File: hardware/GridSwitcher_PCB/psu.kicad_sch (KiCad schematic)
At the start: 36 parts, among them IC1 INA237AIDGSR, IC2 UCC27536DBVR, IC6 P3T1755DPZ, J7 +24V, J8 Battery, Q18 IRF4905

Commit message: -enh made some progress on pcb/fp design
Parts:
- removed Q18: IRF4905, Package_TO_SOT_SMD:TO-263-3_TabPin2, symbol Transistor_FET:IRF4905
- added J11: +24V, Connector_PinHeader_2.54mm:PinHeader_1x02_P2.54mm_Vertical, symbol Connector:Conn_01x02_Pin
- added J14: +3.3V, Connector_PinHeader_2.54mm:PinHeader_1x02_P2.54mm_Vertical, symbol Connector:Conn_01x02_Pin
- added J15: +5V, Connector_PinHeader_2.54mm:PinHeader_1x02_P2.54mm_Vertical, symbol Connector:Conn_01x02_Pin
- added Q17: DMP3013SFV, Package_SON:Diodes_PowerDI3333-8, symbol Transistor_FET:DMP3013SFV
- F3, F4, F5: footprint (none) -> Fuse:Fuse_2920_7451Metric_Pad2.10x5.45mm_HandSolder
- IC1: footprint INA237:SOP50P490X110-10N -> Library:SOP50P490X110-10N
- IC2: footprint (none) -> Library:SOT95P280X145-5N
- IC6: footprint (none) -> Library:P3T1755DPZ
- J7: footprint TerminalBlock:TerminalBlock_bornier-2_P5.08mm -> Connector_BarrelJack:BarrelJack_Wuerth_6941xx301002
- L1, L2: footprint (none) -> Inductor_SMD:L_Bourns-SRN4018
- PS1, PS2: footprint (none) -> Library:R78K3305
- R102, R96, R98: footprint (none) -> Resistor_SMD:R_0603_1608Metric_Pad0.98x0.95mm_HandSolder
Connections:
- net +24V: now also J11.1 (Pin_1)
- net +3V3: now also J14.1 (Pin_1)
- net +5V: now also J15.1 (Pin_1)
- net GND: now also J11.2 (Pin_2), J14.2 (Pin_2), J15.2 (Pin_2)
- net at IC2.4 (OUT), R97.2: now also Q17.4 (G)
- net at F4.2, IC2.5 (VDD), R97.1: now also Q17.1 (S), Q17.2 (S), Q17.3 (S)
- net at R99.1: now also Q17.5 (D)

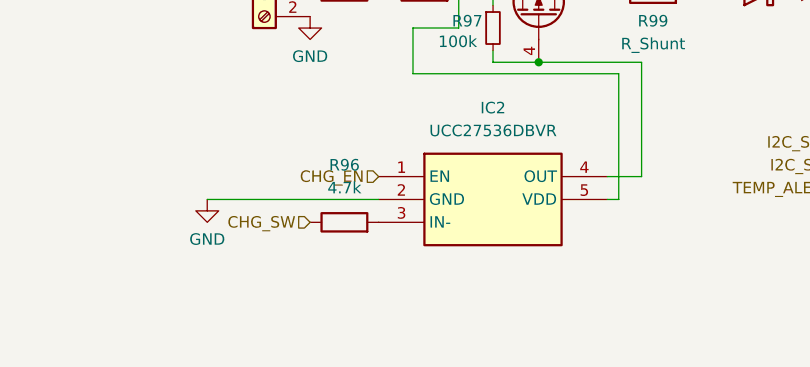
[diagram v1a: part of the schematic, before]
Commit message: -add some changes to schematic, tested the interfaces (uart, spi and i2c) with some test code
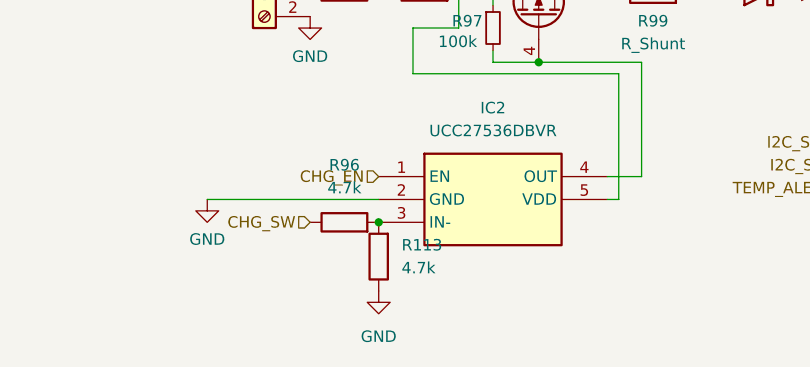
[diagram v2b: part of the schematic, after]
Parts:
- added R113: 4.7k, Resistor_SMD:R_0603_1608Metric_Pad0.98x0.95mm_HandSolder, symbol Device:R
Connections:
- net GND: now also R113.1
- net at IC2.3 (IN-), R96.2: now also R113.2

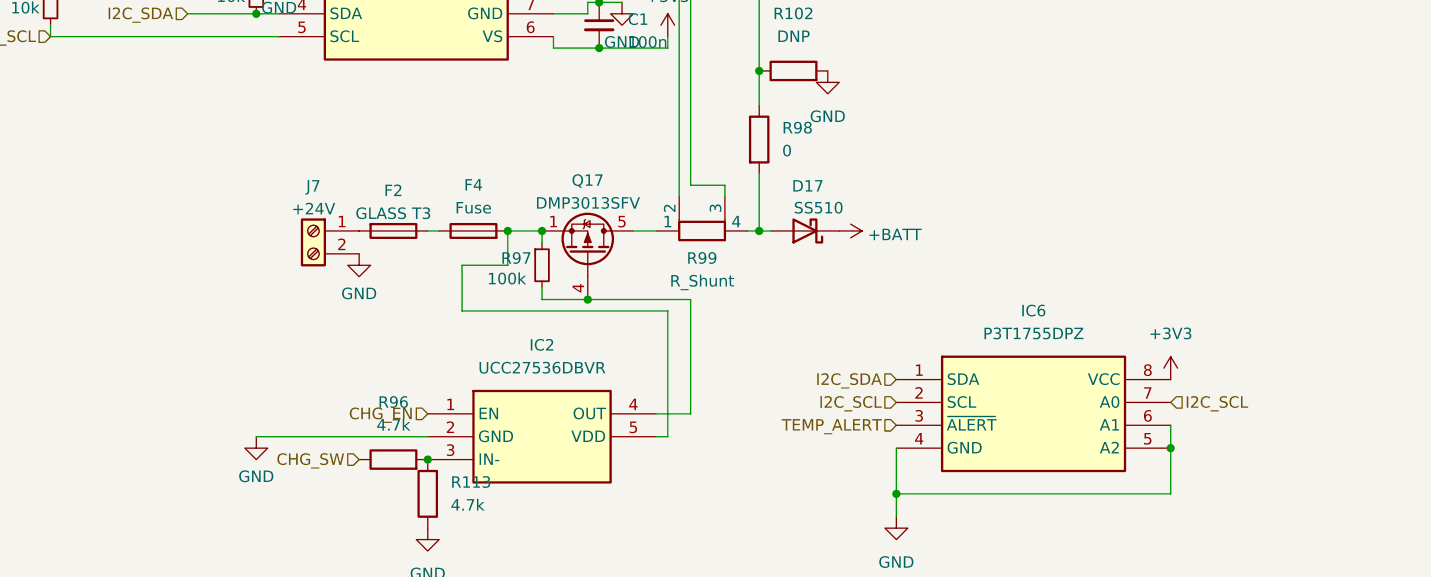
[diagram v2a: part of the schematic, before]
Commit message: -add some more pinning changes, add rts flow control for rs485
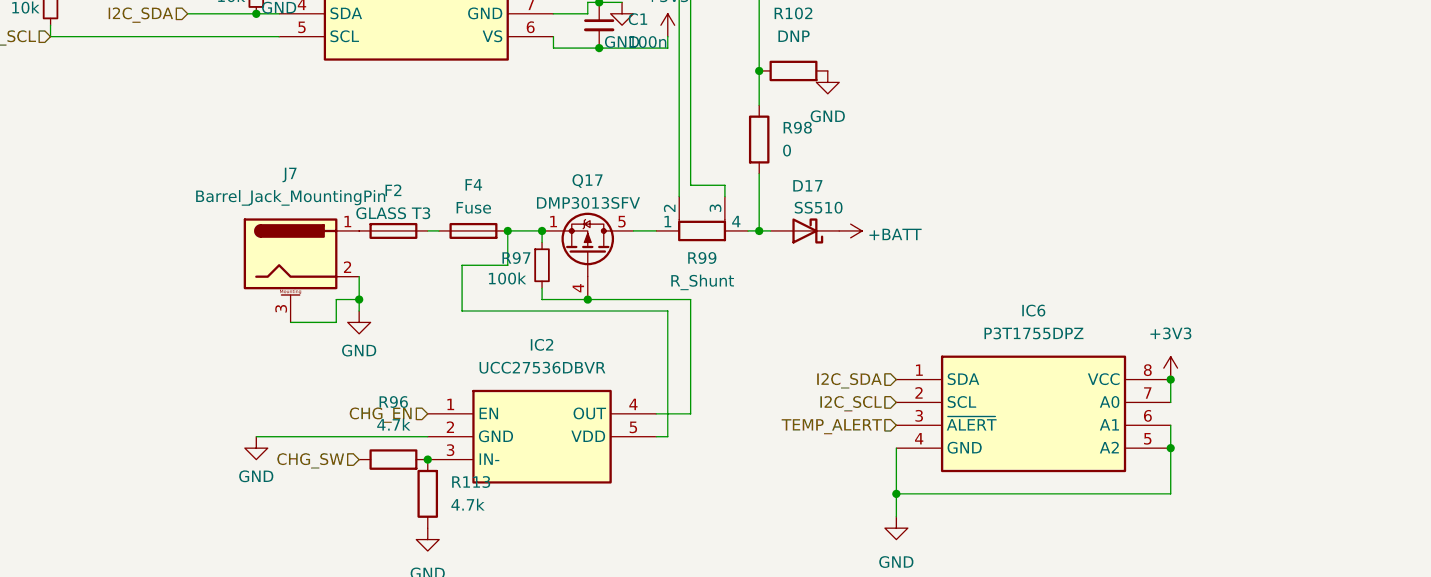
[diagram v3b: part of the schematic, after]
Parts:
- removed J7: +24V, Connector_BarrelJack:BarrelJack_Wuerth_6941xx301002, symbol Connector:Screw_Terminal_01x02
- added J7: Barrel_Jack_MountingPin, Connector_BarrelJack:BarrelJack_Wuerth_6941xx301002, symbol Connector:Barrel_Jack_MountingPin
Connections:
- net +3V3: now also IC6.7 (A0)
- net GND: now also J7.2, J7.3 (MountPin)
- net I2C_SCL: no longer IC6.7 (A0)
- net at F2.2: now also J7.1
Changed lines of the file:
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@@
 	)
 	(junction
+		(at 62.23 114.3)
+		(diameter 0)
+		(color 0 0 0 0)
+	)
+	(junction
 		(at 88.9 86.36)
 		(diameter 0)
@@
 	)
 	(junction
+		(at 152.4 123.19)
+		(diameter 0)
+		(color 0 0 0 0)
+	)
+	(junction
 		(at 194.31 44.45)
 		(diameter 0)
@@
 	(wire
 		(pts
+			(xy 59.69 116.84) (xy 59.69 114.3)
+		)
+		(stroke
+			(width 0)
+			(type default)
+		)
+	)
+	(wire
+		(pts
 			(xy 215.9 49.53) (xy 218.44 49.53)
 		)
@@
 	(wire
 		(pts
+			(xy 54.61 116.84) (xy 59.69 116.84)
+		)
+		(stroke
+			(width 0)
+			(type default)
+		)
+	)
+	(wire
+		(pts
 			(xy 118.11 43.18) (xy 116.84 43.18)
 		)
@@
 	(wire
 		(pts
+			(xy 62.23 115.57) (xy 62.23 114.3)
+		)
+		(stroke
+			(width 0)
+			(type default)
+		)
+	)
+	(wire
+		(pts
 			(xy 87.63 114.3) (xy 99.06 114.3)
 		)
@@
 	(wire
 		(pts
+			(xy 62.23 114.3) (xy 62.23 111.76)
+		)
+		(stroke
+			(width 0)
+			(type default)
+		)
+	)
+	(wire
+		(pts
 			(xy 27.94 85.09) (xy 27.94 83.82)
 		)
@@
 	(wire
 		(pts
+			(xy 59.69 114.3) (xy 62.23 114.3)
+		)
+		(stroke
+			(width 0)
+			(type default)
+		)
+	)
+	(wire
+		(pts
 			(xy 152.4 128.27) (xy 152.4 130.81)
 		)
@@
 	(wire
 		(pts
+			(xy 152.4 123.19) (xy 152.4 125.73)
+		)
+		(stroke
+			(width 0)
+			(type default)
+		)
+	)
+	(wire
+		(pts
 			(xy 45.72 78.74) (xy 45.72 80.01)
 		)
@@
 		)
 	)
-	(hierarchical_label "I2C_SCL"
-		(shape input)
-		(at 152.4 125.73 0)
-		(fields_autoplaced yes)
-		(effects
-			(font
-				(size 1.27 1.27)
-			)
-			(justify left)
-		)
-	)
 	(hierarchical_label "I2C_SDA"
 		(shape input)
@@
 	)
 	(symbol
-		(lib_id "Connector:Screw_Terminal_01x02")
-		(at 57.15 106.68 0)
-		(mirror y)
+		(lib_id "power:+3V3")
+		(at 163.83 49.53 270)
 		(unit 1)
 		(exclude_from_sim no)
@@
 		(dnp no)
 		(fields_autoplaced yes)
-		(property "Reference" "J7"
-			(at 57.15 101.7102 0)
+		(property "Reference" "#PWR0135"
+			(at 160.02 49.53 0)
 			(effects
 				(font
 					(size 1.27 1.27)
 				)
+				(hide yes)
 			)
 		)
-		(property "Value" "+24V"
-			(at 57.15 104.2471 0)
+		(property "Value" "+3V3"
+			(at 167.005 49.53 90)
 			(effects
 				(font
 					(size 1.27 1.27)
 				)
+				(justify left)
 			)
 		)
-		(property "Footprint" "Connector_BarrelJack:BarrelJack_Wuerth_6941xx301002"
-			(at 57.15 106.68 0)
+		(property "Footprint" ""
+			(at 163.83 49.53 0)
 			(effects
 				(font
@@
 			)
 		)
-		(property "Datasheet" "~"
-			(at 57.15 106.68 0)
+		(property "Datasheet" ""
+			(at 163.83 49.53 0)
 			(effects
 				(font
@@
 		)
 		(property "Description" ""
-			(at 57.15 106.68 0)
+			(at 163.83 49.53 0)
 			(effects
 				(font
@@
 		(pin "1"
 		)
-		(pin "2"
-		)
 		(instances
 			(project "GridSwitcher_PCB"
 				(path "/85d790fa-2a68-4a26-9dd2-3e7bd6cf9669/1dd50b27-f3df-4f7a-9d11-22d683709e54"
-					(reference "J7")
+					(reference "#PWR0135")
 					(unit 1)
 				)
@@
 	)
 	(symbol
-		(lib_id "power:+3V3")
-		(at 163.83 49.53 270)
+		(lib_id "Transistor_FET:DMP3013SFV")
+		(at 87.63 109.22 270)
+		(mirror x)
 		(unit 1)
 		(exclude_from_sim no)
@@
 		(dnp no)
 		(fields_autoplaced yes)
-		(property "Reference" "#PWR0135"
-			(at 160.02 49.53 0)
+		(property "Reference" "Q17"
+			(at 87.63 101.0752 90)
 			(effects
 				(font
 					(size 1.27 1.27)
 				)
-				(hide yes)
 			)
 		)
-		(property "Value" "+3V3"
-			(at 167.005 49.53 90)
+		(property "Value" "DMP3013SFV"
+			(at 87.63 103.6121 90)
 			(effects
 				(font
 					(size 1.27 1.27)
 				)
-				(justify left)
 			)
 		)
-		(property "Footprint" ""
-			(at 163.83 49.53 0)
+		(property "Footprint" "Package_SON:Diodes_PowerDI3333-8"
+			(at 85.725 104.14 0)
 			(effects
 				(font
 					(size 1.27 1.27)
+					(italic yes)
 				)
+				(justify left)
 				(hide yes)
 			)
 		)
-		(property "Datasheet" ""
-			(at 163.83 49.53 0)
+		(property "Datasheet" "https://www.diodes.com/assets/Datasheets/DMP3013SFV.pdf"
+			(at 87.63 109.22 90)
 			(effects
 				(font
 					(size 1.27 1.27)
 				)
+				(justify left)
 				(hide yes)
 			)
 		)
 		(property "Description" ""
-			(at 163.83 49.53 0)
+			(at 87.63 109.22 0)
 			(effects
 				(font
@@
 		(pin "1"
 		)
+		(pin "2"
+		)
+		(pin "3"
+		)
+		(pin "4"
+		)
+		(pin "5"
+		)
 		(instances
 			(project "GridSwitcher_PCB"
 				(path "/85d790fa-2a68-4a26-9dd2-3e7bd6cf9669/1dd50b27-f3df-4f7a-9d11-22d683709e54"
-					(reference "#PWR0135")
+					(reference "Q17")
 					(unit 1)
 				)
@@
 	)
 	(symbol
-		(lib_id "Transistor_FET:DMP3013SFV")
-		(at 87.63 109.22 270)
-		(mirror x)
+		(lib_id "Connector:Barrel_Jack_MountingPin")
+		(at 54.61 109.22 0)
 		(unit 1)
 		(exclude_from_sim no)
@@
 		(dnp no)
 		(fields_autoplaced yes)
-		(property "Reference" "Q17"
-			(at 87.63 101.0752 90)
+		(property "Reference" "J7"
+			(at 54.61 100.33 0)
 			(effects
 				(font
@@
 			)
 		)
-		(property "Value" "DMP3013SFV"
-			(at 87.63 103.6121 90)
+		(property "Value" "Barrel_Jack_MountingPin"
+			(at 54.61 102.87 0)
 			(effects
 				(font
@@
 			)
 		)
-		(property "Footprint" "Package_SON:Diodes_PowerDI3333-8"
-			(at 85.725 104.14 0)
+		(property "Footprint" "Connector_BarrelJack:BarrelJack_Wuerth_6941xx301002"
+			(at 55.88 110.236 0)
 			(effects
 				(font
 					(size 1.27 1.27)
-					(italic yes)
 				)
-				(justify left)
 				(hide yes)
 			)
 		)
-		(property "Datasheet" "https://www.diodes.com/assets/Datasheets/DMP3013SFV.pdf"
-			(at 87.63 109.22 90)
+		(property "Datasheet" "~"
+			(at 55.88 110.236 0)
 			(effects
 				(font
 					(size 1.27 1.27)
 				)
-				(justify left)
 				(hide yes)
 			)
 		)
-		(property "Description" ""
-			(at 87.63 109.22 0)
+		(property "Description" "DC Barrel Jack with a mounting pin"
+			(at 54.61 109.22 0)
 			(effects
 				(font
@@
 		(pin "1"
 		)
-		(pin "2"
-		)
 		(pin "3"
 		)
-		(pin "4"
-		)
-		(pin "5"
+		(pin "2"
 		)
 		(instances
-			(project "GridSwitcher_PCB"
+			(project ""
 				(path "/85d790fa-2a68-4a26-9dd2-3e7bd6cf9669/1dd50b27-f3df-4f7a-9d11-22d683709e54"
-					(reference "Q17")
+					(reference "J7")
 					(unit 1)
 				)
@@
 		(lib_name "GND_1")
 		(lib_id "power:GND")
-		(at 62.23 109.22 0)
+		(at 62.23 115.57 0)
 		(unit 1)
 		(exclude_from_sim no)
@@
 		(fields_autoplaced yes)
 		(property "Reference" "#PWR088"
-			(at 62.23 115.57 0)
+			(at 62.23 121.92 0)
 			(effects
 				(font
@@
 		)
 		(property "Value" "GND"
-			(at 62.23 113.6634 0)
+			(at 62.23 120.0134 0)
 			(effects
 				(font
@@
 		)
 		(property "Footprint" ""
-			(at 62.23 109.22 0)
+			(at 62.23 115.57 0)
 			(effects
 				(font
@@
 		)
 		(property "Datasheet" ""
-			(at 62.23 109.22 0)
+			(at 62.23 115.57 0)
 			(effects
 				(font
@@
 		)
 		(property "Description" ""
-			(at 62.23 109.22 0)
+			(at 62.23 115.57 0)
 			(effects
 				(font

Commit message: -enh final revision; ordered
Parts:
- removed F4: Fuse, Fuse:Fuse_2920_7451Metric_Pad2.10x5.45mm_HandSolder, symbol Device:Fuse
- removed R113: 4.7k, Resistor_SMD:R_0603_1608Metric_Pad0.98x0.95mm_HandSolder, symbol Device:R
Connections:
- net at IC2.5 (VDD), Q17.1 (S), Q17.2 (S)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: now also F2.1
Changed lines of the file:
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@@
 	)
 	(junction
-		(at 69.85 132.08)
+		(at 121.92 135.89)
 		(diameter 0)
 		(color 0 0 0 0)
 	)
 	(junction
-		(at 121.92 135.89)
+		(at 45.72 80.01)
 		(diameter 0)
 		(color 0 0 0 0)
 	)
 	(junction
-		(at 45.72 80.01)
+		(at 127 43.18)
 		(diameter 0)
 		(color 0 0 0 0)
 	)
 	(junction
-		(at 127 43.18)
+		(at 78.74 106.68)
 		(diameter 0)
 		(color 0 0 0 0)
@@
 	)
 	(junction
-		(at 78.74 106.68)
-		(diameter 0)
-		(color 0 0 0 0)
-	)
-	(junction
 		(at 50.8 82.55)
 		(diameter 0)
@@
 	(wire
 		(pts
-			(xy 69.85 106.68) (xy 71.12 106.68)
+			(xy 69.85 106.68) (xy 78.74 106.68)
 		)
 		(stroke
@@
 	)
 	(symbol
-		(lib_id "Device:Fuse")
-		(at 74.93 106.68 90)
-		(unit 1)
-		(exclude_from_sim no)
-		(in_bom yes)
-		(on_board yes)
-		(dnp no)
-		(fields_autoplaced yes)
-		(property "Reference" "F4"
-			(at 74.93 101.6 90)
-			(effects
-				(font
-					(size 1.27 1.27)
-				)
-			)
-		)
-		(property "Value" "Fuse"
-			(at 74.93 104.14 90)
-			(effects
-				(font
-					(size 1.27 1.27)
-				)
-			)
-		)
-		(property "Footprint" "Fuse:Fuse_2920_7451Metric_Pad2.10x5.45mm_HandSolder"
-			(at 74.93 108.458 90)
-			(effects
-				(font
-					(size 1.27 1.27)
-				)
-				(hide yes)
-			)
-		)
-		(property "Datasheet" "~"
-			(at 74.93 106.68 0)
-			(effects
-				(font
-					(size 1.27 1.27)
-				)
-				(hide yes)
-			)
-		)
-		(property "Description" ""
-			(at 74.93 106.68 0)
-			(effects
-				(font
-					(size 1.27 1.27)
-				)
-				(hide yes)
-			)
-		)
-		(pin "1"
-		)
-		(pin "2"
-		)
-		(instances
-			(project "GridSwitcher_PCB"
-				(path "/85d790fa-2a68-4a26-9dd2-3e7bd6cf9669/1dd50b27-f3df-4f7a-9d11-22d683709e54"
-					(reference "F4")
-					(unit 1)
-				)
-			)
-		)
-	)
-	(symbol
 		(lib_id "Device:L")
 		(at 199.39 44.45 90)
@@
 	)
 	(symbol
-		(lib_name "GND_5")
-		(lib_id "power:GND")
-		(at 69.85 139.7 0)
-		(unit 1)
-		(exclude_from_sim no)
-		(in_bom yes)
-		(on_board yes)
-		(dnp no)
-		(fields_autoplaced yes)
-		(property "Reference" "#PWR0141"
-			(at 69.85 146.05 0)
-			(effects
-				(font
-					(size 1.27 1.27)
-				)
-				(hide yes)
-			)
-		)
-		(property "Value" "GND"
-			(at 69.85 144.78 0)
-			(effects
-				(font
-					(size 1.27 1.27)
-				)
-			)
-		)
-		(property "Footprint" ""
-			(at 69.85 139.7 0)
-			(effects
-				(font
-					(size 1.27 1.27)
-				)
-				(hide yes)
-			)
-		)
-		(property "Datasheet" ""
-			(at 69.85 139.7 0)
-			(effects
-				(font
-					(size 1.27 1.27)
-				)
-				(hide yes)
-			)
-		)
-		(property "Description" "Power symbol creates a global label with name \"GND\" , ground"
-			(at 69.85 139.7 0)
-			(effects
-				(font
-					(size 1.27 1.27)
-				)
-				(hide yes)
-			)
-		)
-		(pin "1"
-		)
-		(instances
-			(project ""
-				(path "/85d790fa-2a68-4a26-9dd2-3e7bd6cf9669/1dd50b27-f3df-4f7a-9d11-22d683709e54"
-					(reference "#PWR0141")
-					(unit 1)
-				)
-			)
-		)
-	)
-	(symbol
 		(lib_id "power:GND")
 		(at 121.92 138.43 0)
@@
 					(unit 1)
 				)
-			)
-		)
-	)
-	(symbol
-		(lib_id "Device:R")
-		(at 69.85 135.89 180)
-		(unit 1)
-		(exclude_from_sim no)
-		(in_bom yes)
-		(on_board yes)
-		(dnp no)
-		(fields_autoplaced yes)
-		(property "Reference" "R113"
-			(at 72.39 134.6199 0)
-			(effects
-				(font
-					(size 1.27 1.27)
-				)
-				(justify right)
-			)
-		)
-		(property "Value" "4.7k"
-			(at 72.39 137.1599 0)
-			(effects
-				(font
-					(size 1.27 1.27)
-				)
-				(justify right)
-			)
-		)
-		(property "Footprint" "Resistor_SMD:R_0603_1608Metric_Pad0.98x0.95mm_HandSolder"
-			(at 71.628 135.89 90)
-			(effects
-				(font
-					(size 1.27 1.27)
-				)
-				(hide yes)
-			)
-		)
-		(property "Datasheet" "~"
-			(at 69.85 135.89 0)
-			(effects
-				(font
-					(size 1.27 1.27)
-				)
-				(hide yes)
-			)
-		)
-		(property "Description" ""
-			(at 69.85 135.89 0)
-			(effects
-				(font
-					(size 1.27 1.27)
-				)
-				(hide yes)
-			)
-		)
-		(pin "1"
-		)
-		(pin "2"
-		)
-		(instances
-			(project "GridSwitcher_PCB"
-				(path "/85d790fa-2a68-4a26-9dd2-3e7bd6cf9669/1dd50b27-f3df-4f7a-9d11-22d683709e54"
-					(reference "R113")
-					(unit 1)
-				)
